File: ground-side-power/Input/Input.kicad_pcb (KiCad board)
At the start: 2 copper layers, 95.8 x 122.1 mm, 41 parts, among them J1 Battery Terminals, J2 Battery Terminals, J26 Conn_01x02_Female, J3 Battery Terminals, J4 Battery Terminals, J5 874270842, J6 874270842, J7 ATX-24, J8 Conn_01x03_Female, J9 Conn_01x03_Female, K1 AZ2150-1A-12DEF, M1 Fan_PC_Chassis, SW1 GRB234A2NABA1, U1 INA180, U2 INA180

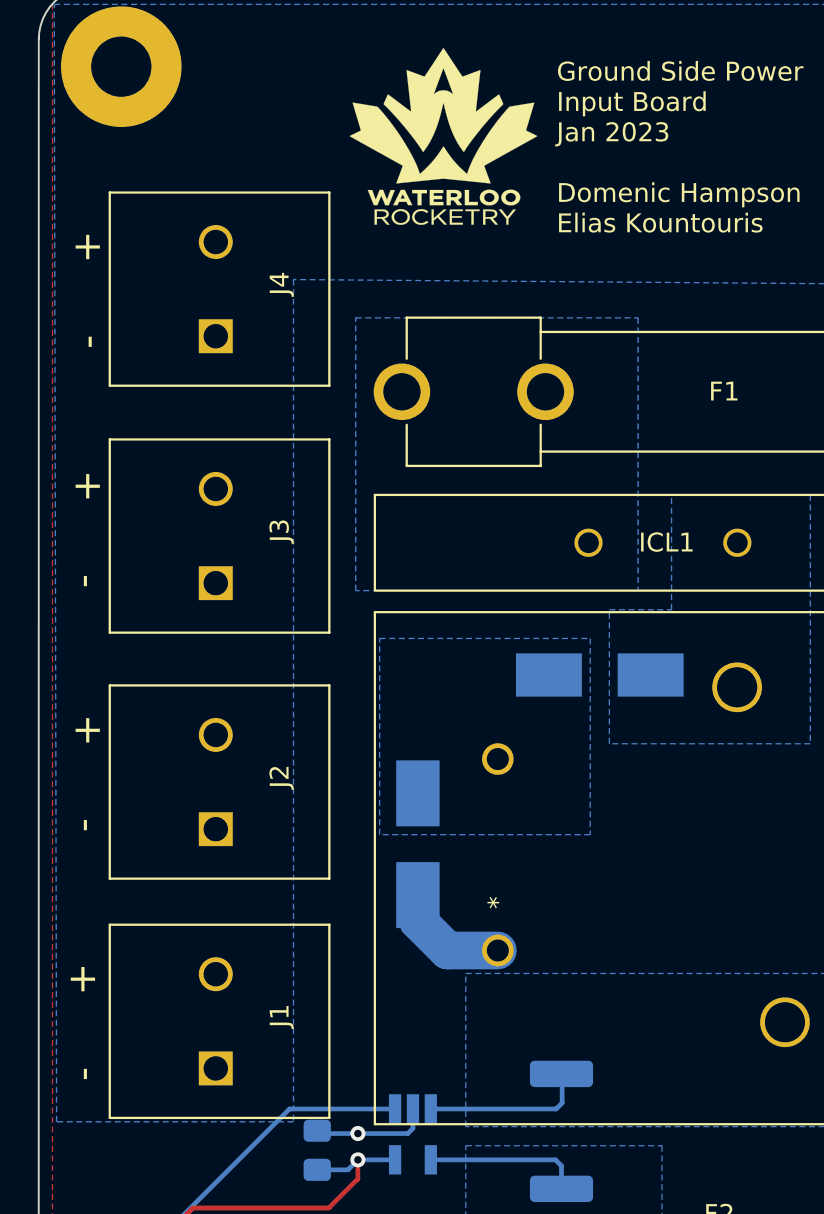
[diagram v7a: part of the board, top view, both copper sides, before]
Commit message: resolved issues from testing
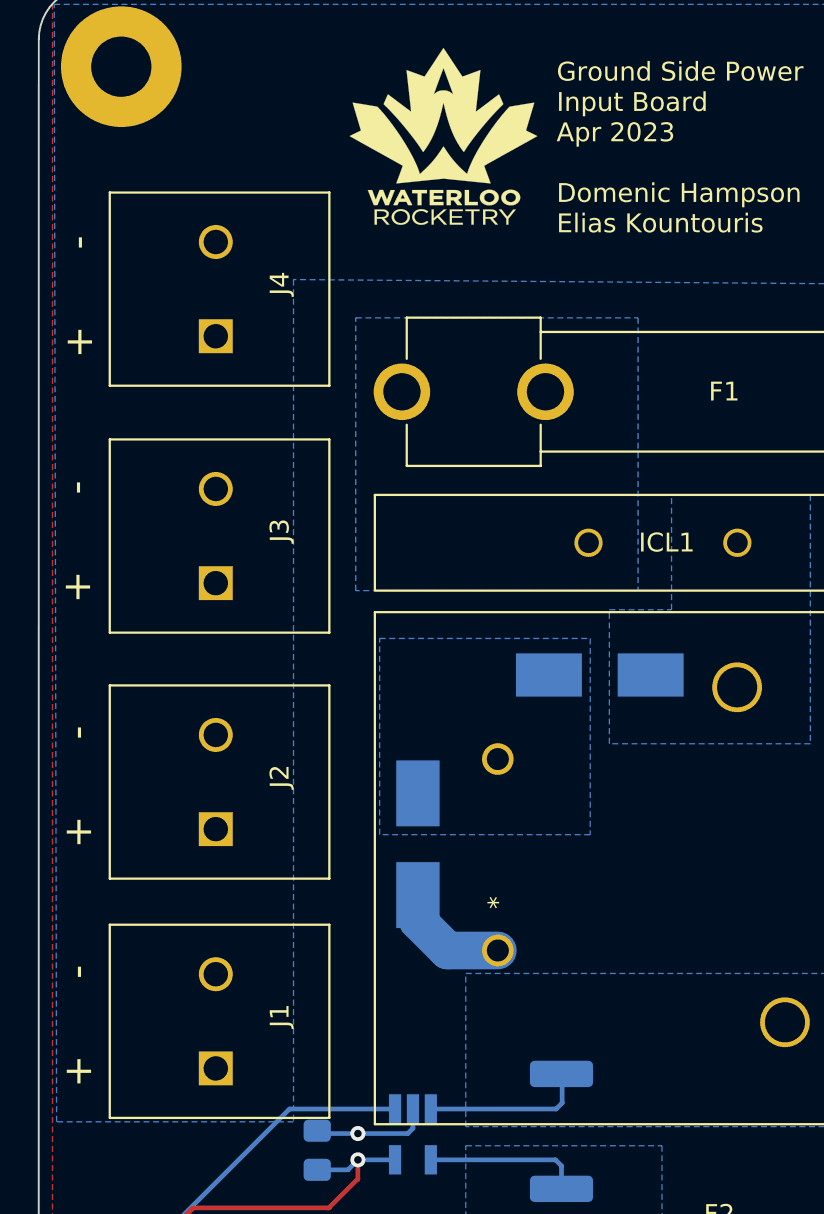
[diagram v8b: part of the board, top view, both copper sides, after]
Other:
- board text added: "Ground Side Power Input Board Apr 2023 Domenic Hampson Elias Kountouris"
- board text removed: "Ground Side Power Input Board Jan 2023 Domenic Hampson Elias Kountouris"
